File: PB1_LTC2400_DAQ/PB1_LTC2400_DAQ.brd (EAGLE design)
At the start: 100 x 80 mm, 0 parts

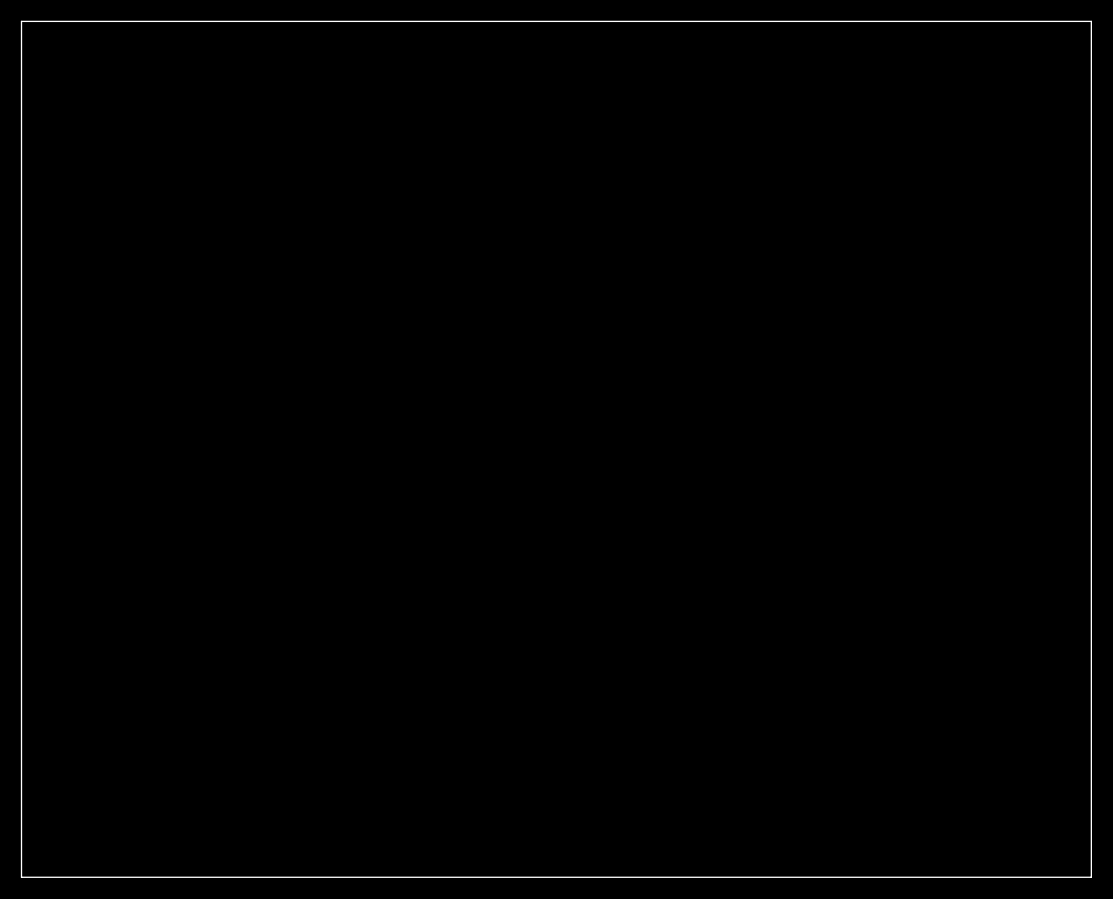
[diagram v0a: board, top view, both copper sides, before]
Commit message: * updated PB1 board, need a lot more lessons learned with it, so lets leave it for now * updated LTC2400 test board, going to focus on that first
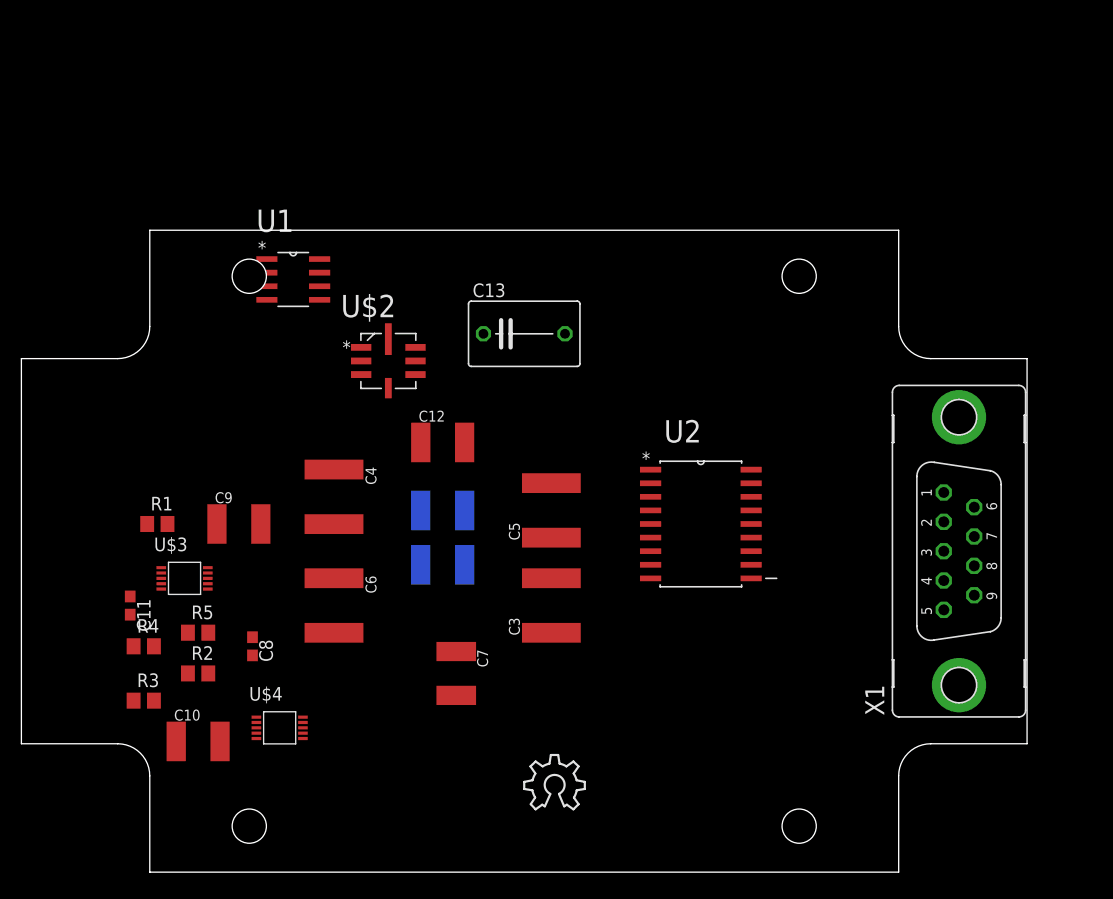
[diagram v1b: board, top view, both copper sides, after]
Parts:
- added C1, C10, C12, C2, C7, C9: 100n, SquantorRCL:C1812K
- added C11, C8: 100n, SquantorRCL:C0603
- added C13: (no value), SquantorRCL:C075-063X106
- added C3, C4, C5, C6: 1u, SquantorRCL:C2220K
- added LOGO1: OSHW_LOGO_8MILX0200-NT, ohw-logo:OSHW_8X200_NOTEXT
- added R1, R2: 0, SquantorRCL:R0805
- added R3, R5: 1k, SquantorRCL:R0805
- added R4: 20k, SquantorRCL:R0805
- added U$1: FUTURLEC_PB1PB1, SquantorPCBOutline:FUTURLEC_PB1
- added U$2: LTC6655LS8_ELONG, SquantorLinearTechnology:LS8_ELONG
- added U$3, U$4: LTC2057, SquantorLinearTechnology:MS-MSOP10
- added U1: LTC2400CS8PBF, SquantorLinearTechnology:SOIC127P600X175-8N
- added U2: LTC1043CSWPBFSW, SquantorLinearTechnology:SOIC127P1032X264-18N
- added X1: (no value), con-subd:F09VP
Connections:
- new net +5V: C1.1, C10.1, C12.1, C9.1, U$2.1, U$2.2, U$3.8, U$4.8, U1.1, U2.4
- new net -5V: C10.2, C2.1, C7.2, C9.2, U$3.5, U$4.5, U2.17
- new net CA+: C3.1, U2.11
- new net CA-: C3.2, U2.12
- new net CA_GUARD: U2.10
- new net CB+: C4.1, U2.2
- new net CB-: C4.2, U2.3
- new net CB_GUARD: U2.1
- new net COSC: C7.1, U2.16
- new net DIFF_IN_1: U2.7
- new net DIFF_IN_2: U2.13
- new net GND: C1.2, C12.2, C13.1, C2.2, C5.2, U$2.3, U$2.4, U$2.5, U$2.8, U1.4, U2.15
- new net N$1: R5.2, U1.3
- new net N$2: U$4.4
- new net N$5: U$4.1
- new net OUT_AMP: R4.2, R5.1, U$4.6
- new net OUT_BUF: R2.2, R3.1, U$3.6
- new net SDCOM_AMP: C8.2, U$4.9
- new net SDCOM_BUF: C11.2, U$3.9
- new net SD_AMP: C8.1, U$4.10
- new net SD_BUF: C11.1, U$3.10
- new net V+_AMP: U$4.3
- new net V+_BUF: R1.2, U$3.3
- new net V-_AMP: R3.2, R4.1, U$4.2
- new net V-_BUF: R2.1, U$3.2, U$3.4
- new net VOUT: C6.1, U2.8
- new net VREF: C13.2, U$2.6, U$2.7, U1.2, U2.6
- new net VREF/2: C5.1, C6.2, R1.1, U2.14, U2.18, U2.5
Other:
- board size 100 x 80 mm -> 94 x 60 mm
